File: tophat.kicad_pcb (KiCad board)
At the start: 2 copper layers, 68.6 x 53.3 mm, 26 parts, among them J1 Power, J2 Digital/PWM, J3 Analog, J4 Digital/PWM, J5 Conn_01x03_Socket, J6 Conn_01x03_Socket, J7 Conn_01x03_Socket, U1 74LVC2G241, U2 TXB0104PW

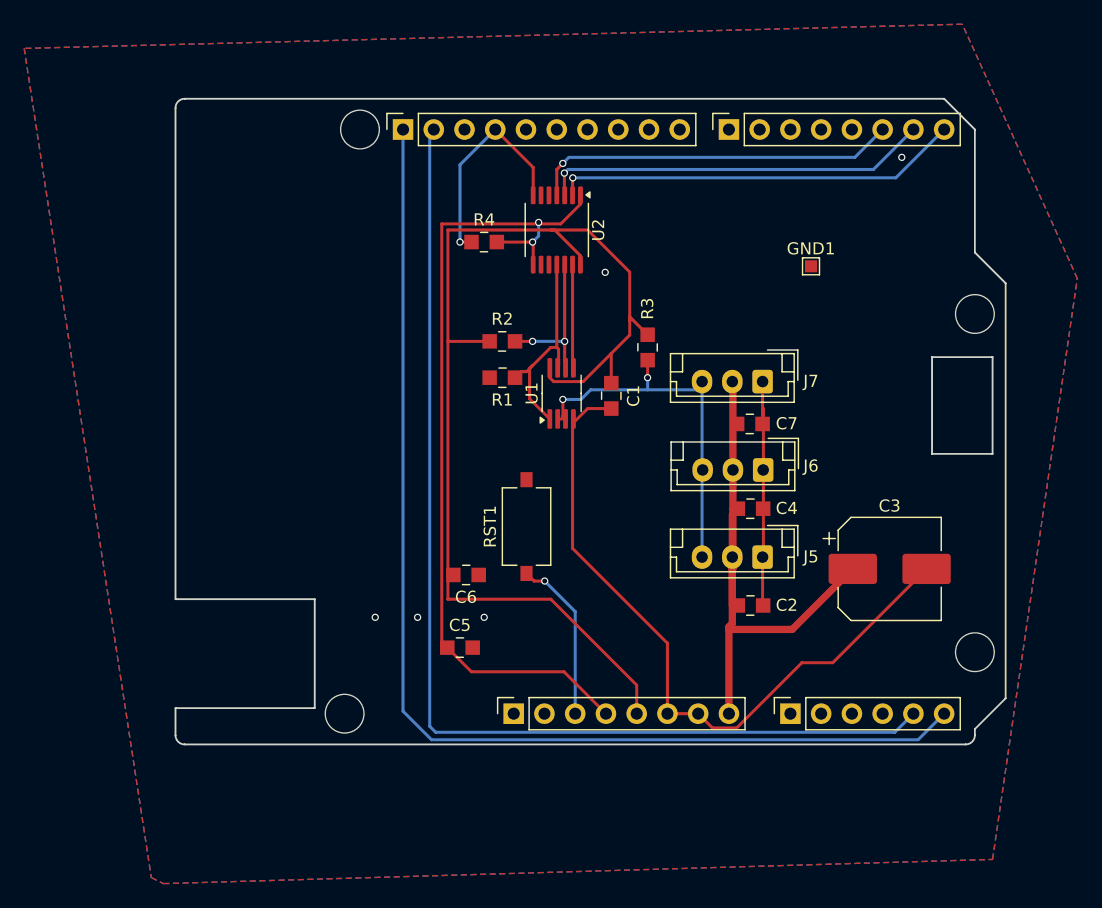
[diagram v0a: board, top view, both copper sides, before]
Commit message: Add silk screen and fix up schematic
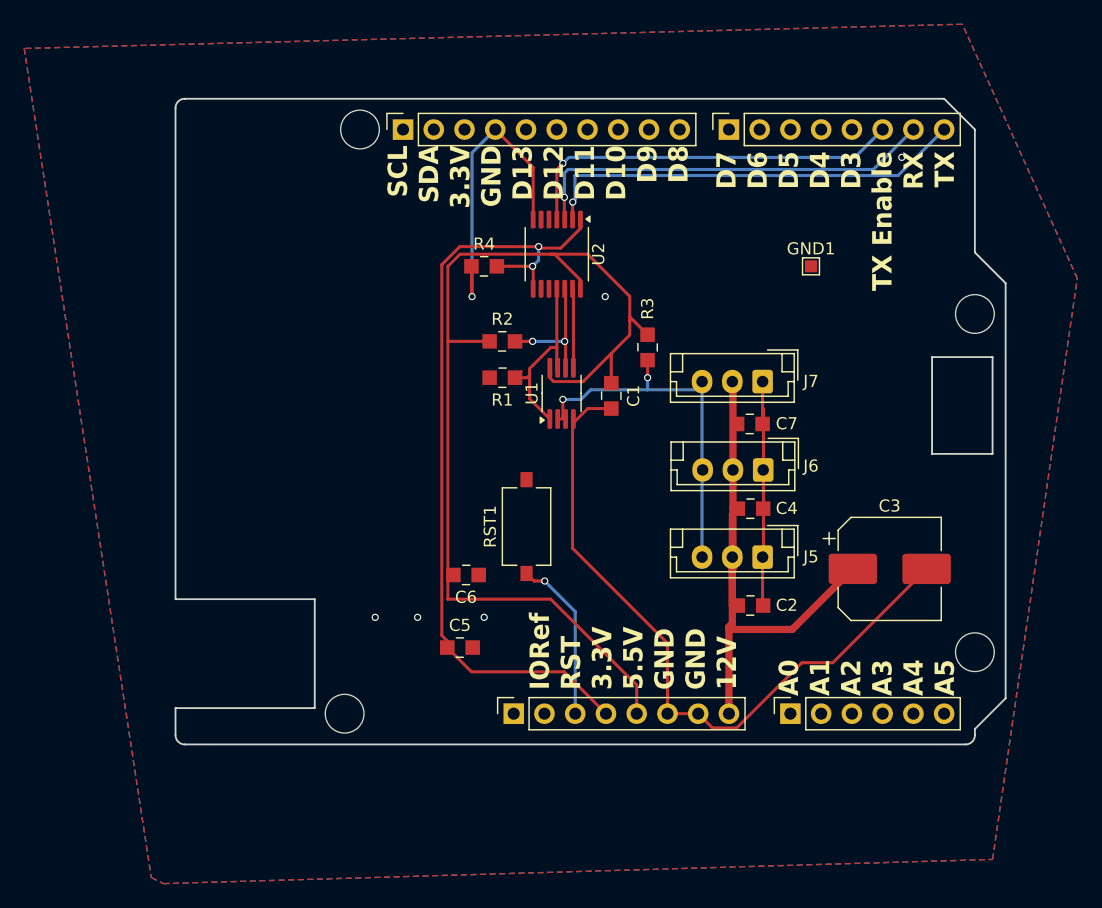
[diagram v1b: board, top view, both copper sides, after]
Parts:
- moved R4 2.00 mm to (125.5, 60.5)
- moved U2 2.00 mm to (131.5, 59.5)
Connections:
- J3 pad 5: /SDA/A4 -> /A4
- J3 pad 6: /SCL/A5 -> /A5
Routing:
- net /SCL/A5: track 94.6 -> 0.00 mm
- net /SDA/A4: track 89.8 -> 0.00 mm
- net GND: track 96.3 -> 104.0 mm
- net 5v: track 94.6 -> 89.7 mm
- net 3.3v: track 69.2 -> 67.0 mm
- net TX3.3v: track 33.8 -> 35.8 mm
- net TXEnable3.3v: track 30.4 -> 32.4 mm
- net RX3.3v: track 32.1 -> 34.1 mm
- net TX5v: track 8.26 -> 6.55 mm
- net RX5v: track 11.8 -> 10.2 mm
- net TX_Enable_5v: track 18.2 -> 16.7 mm
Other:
- board text added: "A0 A1 A2 A3 A4 A5"
- board text added: "D7 D6 D5 D4 D3 TX Enable RX TX"
- board text added: "IORef RST 3.3V 5.5V GND GND 12V"
- board text added: "SCL SDA 3.3V GND D13 D12 D11 D10 D9 D8"
